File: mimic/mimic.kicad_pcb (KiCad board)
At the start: 2 copper layers, 82.6 x 27.6 mm, 61 parts, among them J1 SMA, J2 SMA, J3 SMA, J4 SMA, U1 XCO, U2 AD9835, U3 AD9835, U4 HMC595, U5 HMC595, U6 teensy_3.1

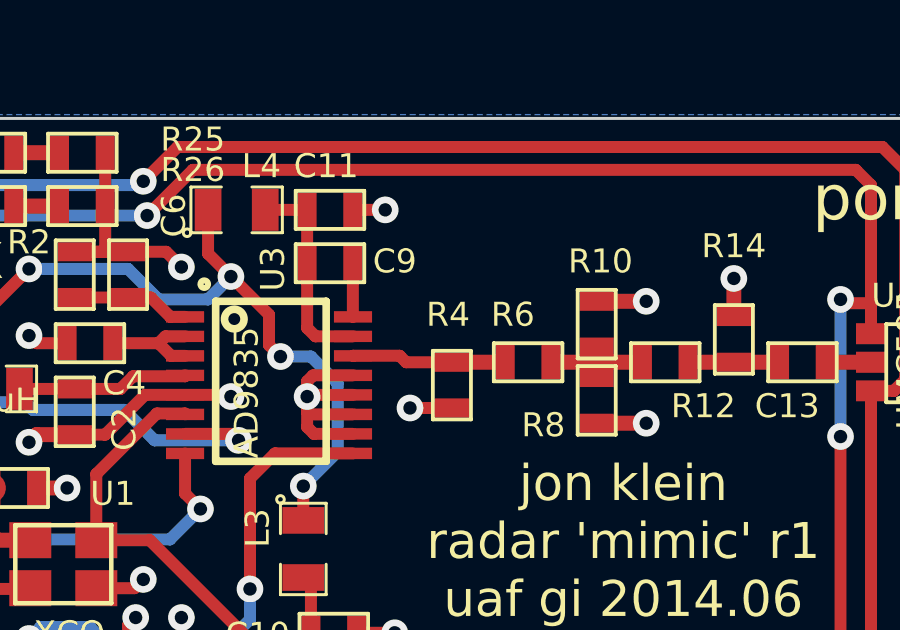
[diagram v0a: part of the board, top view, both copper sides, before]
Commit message: picked tx hptr diode bias with higher linearity, added missing resistors for coupler in control board
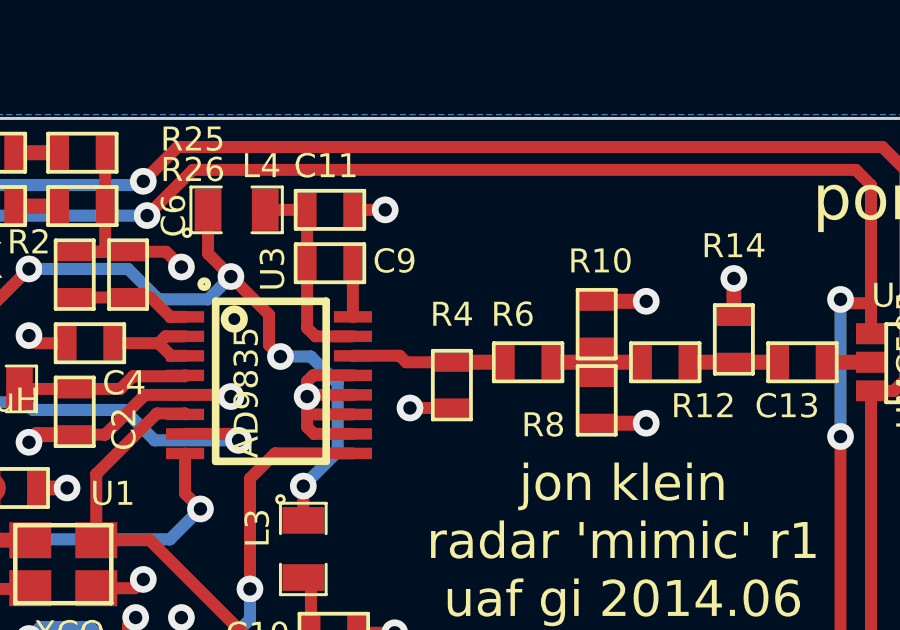
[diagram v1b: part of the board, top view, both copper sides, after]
